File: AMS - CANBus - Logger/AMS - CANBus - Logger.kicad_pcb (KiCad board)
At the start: 2 copper layers, 72.9 x 71.1 mm, 46 parts, among them IC2 OPA4340UA, J1 Power_And_CAN, J2 Power_And_CAN, J3 TTL_Programmer, J4 ICSP, J5 Conn_01x02, J6 Screw_Terminal_01x02, Q1 IRF9Z34NPBF, U1 3568, U2 ATmega328P-P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

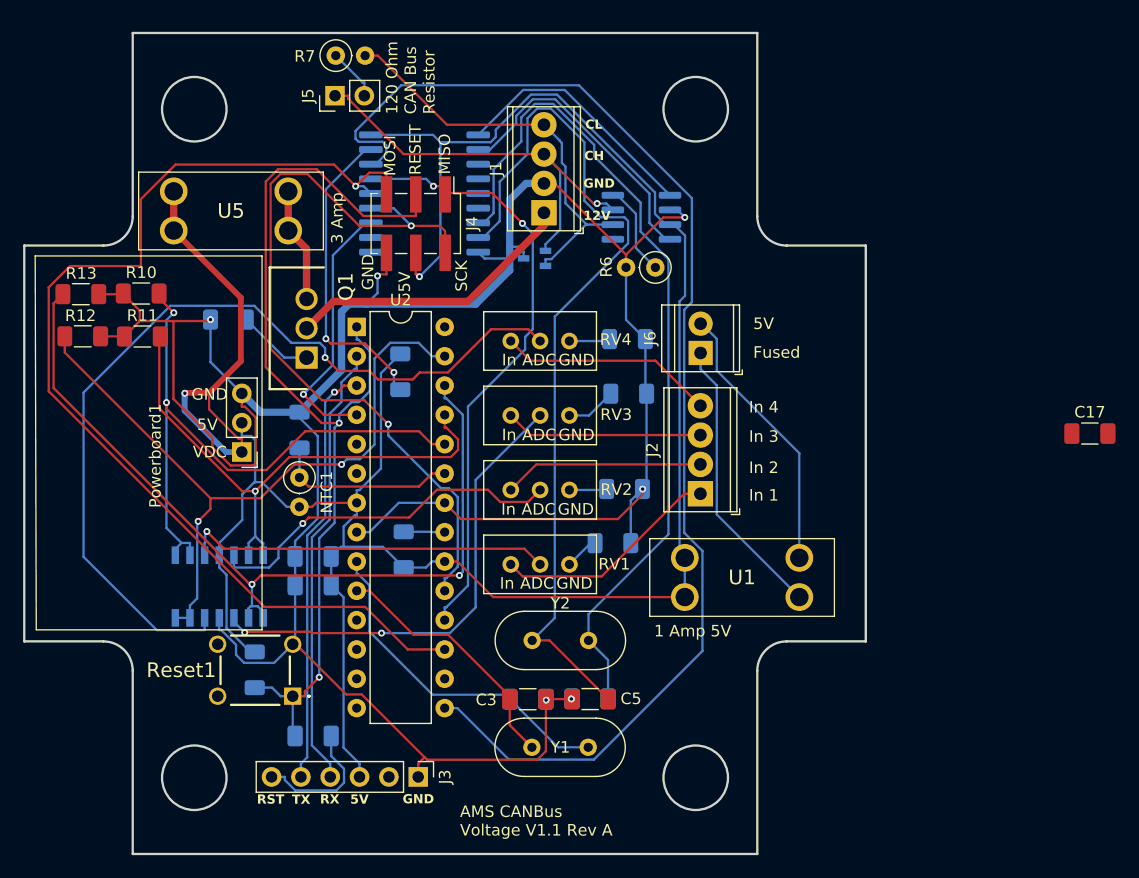
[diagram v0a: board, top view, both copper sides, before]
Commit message: finished the regular format adding the uno shield
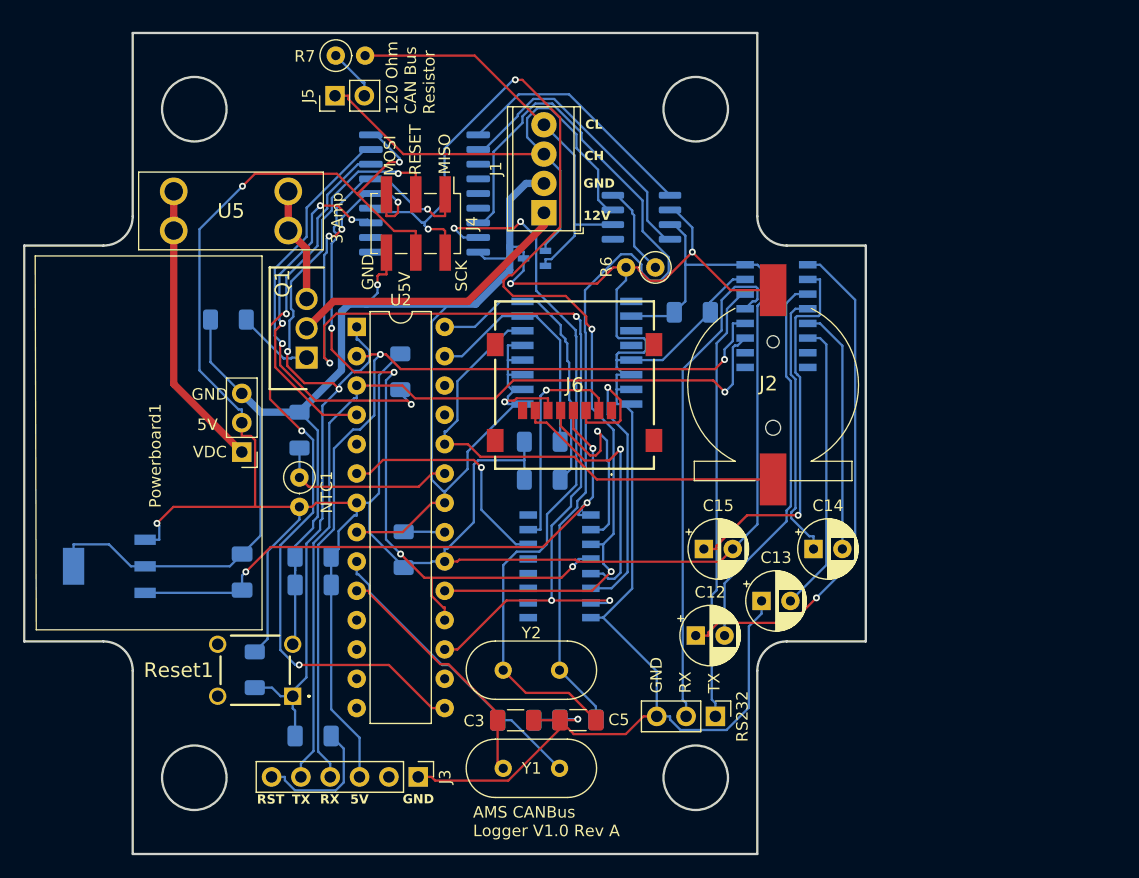
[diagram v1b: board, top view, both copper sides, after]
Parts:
- removed R10, R11, R12, R13: 47K, Resistor_SMD:R_1206_3216Metric_Pad1.30x1.75mm_HandSolder
- removed R14, R15: 1k, Resistor_SMD:R_1206_3216Metric_Pad1.30x1.75mm_HandSolder
- removed RV1, RV2, RV3, RV4: 200k, Potentiometer_THT:Potentiometer_Bourns_3296W_Vertical
- removed U1: 3568, SamacSys_Parts:3568
- added C12: 1uF, Capacitor_THT:CP_Radial_D5.0mm_P2.50mm, F.Cu at (170.3, 108.5)
- added C13: 1uF, Capacitor_THT:CP_Radial_D5.0mm_P2.50mm, F.Cu at (176.0, 105.5)
- added C14: 1uF, Capacitor_THT:CP_Radial_D5.0mm_P2.50mm, F.Cu at (180.5, 101.0)
- added C15: 1uF, Capacitor_THT:CP_Radial_D5.0mm_P2.50mm, F.Cu at (171.0, 101.0)
- added C8: 0.1uF, Capacitor_SMD:C_1206_3216Metric_Pad1.33x1.80mm_HandSolder, B.Cu at (170.0, 80.5)
- added IC1: DS3231SN#, SamacSys:SOIC127P1032X265-16N, B.Cu at (160.0, 84.0)
- added IC4: CD74HC4050ME4, SamacSys:SOIC127P600X175-16N, B.Cu at (158.5, 102.5)
- added IC5: AZ1117CH2-3.3TRG1, SamacSys:SOT230P700X180-4N, B.Cu at (119.5, 102.5)
- added RS232: Conn_01x03, Connector_PinHeader_2.54mm:PinHeader_1x03_P2.54mm_Vertical, F.Cu at (172.0, 115.5)
- C17: moved to B.Cu
- D1: footprint SamacSys_Parts:SOT65P210X110-3N -> SamacSys:SOT65P210X110-3N
- IC2: value OPA4340UA -> MAX232ECSE+T; footprint SamacSys_Parts:SOIC127P600X175-14N -> SamacSys:SOIC127P600X175-16N
- J2: value Power_And_CAN -> S8411-45R; footprint TerminalBlock_Phoenix:TerminalBlock_Phoenix_MPT-0,5-4-2.54_1x04_P2.54mm_Horizontal -> SamacSys:S8411-45R_1
- J6: value Screw_Terminal_01x02 -> GTFH08131YHR; footprint TerminalBlock_TE-Connectivity:TerminalBlock_TE_282834-2_1x02_P2.54mm_Horizontal -> SamacSys:GTFH08131YHR
- Q1: footprint SamacSys_Parts:TO254P469X1042X1967-3P -> SamacSys:TO254P469X1042X1967-3P
- R8, R9: value 1k -> 10k
- Reset1: footprint SamacSys_Parts:TS0266160BK260LCRD -> SamacSys:TS0266160BK260LCRD
- U5: footprint SamacSys_Parts:3568 -> SamacSys:3568
- moved C17 74.4 mm to (131.0, 103.0), turned to -90 degrees
- moved IC2 53.7 mm to (177.3, 80.8), turned to 180 degrees
- moved J2 11.3 mm to (177.0, 86.8), turned to 0 degrees
- moved J6 11.3 mm to (159.8, 86.8), turned to 0 degrees
- moved R8 10.6 mm to (157.0, 95.0)
- moved R9 8.22 mm to (157.0, 91.7)
- moved Y2 3.60 mm to (153.6, 111.5)
- moved Y1 3.08 mm to (153.6, 120.0)
- moved C3 2.11 mm to (154.7, 115.8)
- moved C4 2.11 mm to (160.1, 115.8)
- moved C5 2.11 mm to (160.1, 115.8)
- moved C2 2.11 mm to (154.7, 115.8)
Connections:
- net /BareMinAtmel328P/PB1-D9 renamed CANBusCS
- IC2 pad 1: /BareMinAtmel328P/PC1-A1 -> Net-(IC2-C1+)
- IC2 pad 10: /BufferedADC/ADCIN3 -> unconnected-(IC2-T2IN-Pad10)
- IC2 pad 11: GND -> COMTXTTL
- IC2 pad 12: /BufferedADC/ADCIN4 -> COMRXTTL
- IC2 pad 13: /BareMinAtmel328P/PC4-A4-SDA -> RX232
- IC2 pad 14: /BareMinAtmel328P/PC4-A4-SDA -> TX232
- IC2 pad 2: /BareMinAtmel328P/PC1-A1 -> Net-(IC2-V+)
- IC2 pad 3: /BufferedADC/ADCIN1 -> Net-(IC2-C1-)
- IC2 pad 4: +5V -> Net-(IC2-C2+)
- IC2 pad 5: /BufferedADC/ADCIN2 -> Net-(IC2-C2-)
- IC2 pad 6: /BareMinAtmel328P/PC2-A2 -> Net-(IC2-V-)
- IC2 pad 7: /BareMinAtmel328P/PC2-A2 -> unconnected-(IC2-T2OUT-Pad7)
- IC2 pad 8: /BareMinAtmel328P/PC3-A3 -> unconnected-(IC2-R2IN-Pad8)
- IC2 pad 9: /BareMinAtmel328P/PC3-A3 -> unconnected-(IC2-R2OUT-Pad9)
- J2 pad 1: Net-(J2-Pin_1) -> /BareMinAtmel328P/PC1-A1
- J2 pad 2: Net-(J2-Pin_2) -> GND
- J3 pad 4: /BareMinAtmel328P/PD0-RX -> COMRXTTL
- J3 pad 5: /BareMinAtmel328P/PD1-TX -> COMTXTTL
- J6 pad 1: Net-(J6-Pin_1) -> unconnected-(J6-DAT2-Pad1)
- J6 pad 2: Net-(J6-Pin_2) -> SDCS3.3V
- R8 pad 1: Net-(R8-Pad1) -> +5V
- R8 pad 2: GND -> SCL
- R9 pad 1: Net-(R9-Pad1) -> +5V
- R9 pad 2: GND -> SDA
- U2 pad 14: SDCS5V -> /BareMinAtmel328P/PB0-D8
- U2 pad 2: /BareMinAtmel328P/PD0-RX -> COMRXTTL
- U2 pad 27: /BareMinAtmel328P/PC4-A4-SDA -> SDA
- U2 pad 28: /BareMinAtmel328P/PC5-A5-SCL -> SCL
- U2 pad 3: /BareMinAtmel328P/PD1-TX -> COMTXTTL
- U2 pad 6: /BareMinAtmel328P/PD4-D4 -> SDCS5V
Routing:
- net GND: track 234.1 -> 319.0 mm, vias 6 -> 5
- net COMRXTTL: track 0.00 -> 76.9 mm, vias 0 -> 2
- net /BufferedADC/ADCIN4: track 76.4 -> 0.00 mm, vias 1 -> 0
- net COMTXTTL: track 0.00 -> 75.0 mm, vias 0 -> 1
- net /BareMinAtmel328P/PC3-A3: track 72.6 -> 0.00 mm, vias 2 -> 0
- net /BareMinAtmel328P/PC4-A4-SDA: track 62.3 -> 0.00 mm, vias 2 -> 0
- net +3.3V: track 0.00 -> 53.6 mm, vias 0 -> 3
- net +5V: track 185.0 -> 233.9 mm, vias 1 -> 3
- net /BareMinAtmel328P/PC2-A2: track 47.9 -> 0.00 mm, vias 1 -> 0
- net Net-(IC2-C1+): track 0.00 -> 44.5 mm, vias 0 -> 1
- net RX232: track 0.00 -> 43.6 mm
- net CANBusCS: track 108.6 -> 65.7 mm, vias 0 -> 3
- net /BufferedADC/ADCIN3: track 41.3 -> 0.00 mm, vias 2 -> 0
- net /BareMinAtmel328P/PD0-RX: track 38.8 -> 0.00 mm
- net TX232: track 0.00 -> 38.1 mm
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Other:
- board text added: "AMS CANBus Logger V1.0 Rev A"
- board text removed: "1 Amp 5V"
- board text removed: "ADC"
- board text removed: "AMS CANBus Voltage V1.1 Rev A"
- board text removed: "Fused"
- board text removed: "In"
- board text removed: "In 1"
- board text removed: "In 2"
- board text removed: "In 3"
- board text removed: "In 4"
